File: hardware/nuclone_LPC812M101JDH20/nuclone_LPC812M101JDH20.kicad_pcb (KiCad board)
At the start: 2 copper layers, 48.3 x 48.3 mm, 35 parts, among them J1 JTAG_2X05, J2 Conn_01x02, J3 nuclone_small_left, J4 nuclone_small_right, U1 MCP1702-MB, U2 LPC812M101JDH20, Y1 12MHz

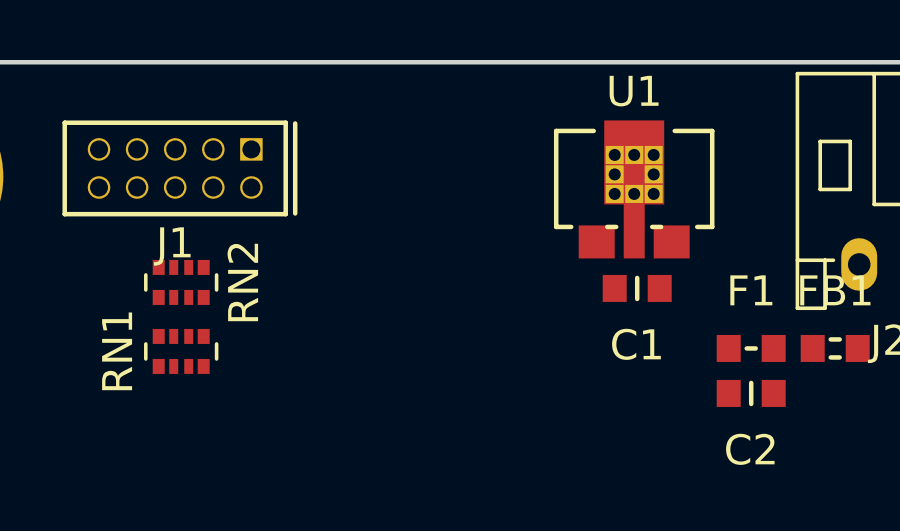
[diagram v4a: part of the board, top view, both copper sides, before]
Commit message: added switch footprints, added reset button
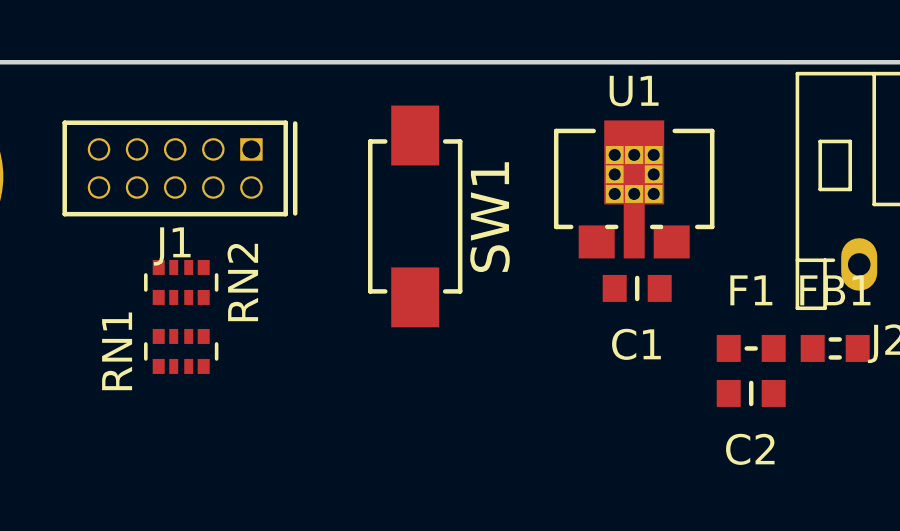
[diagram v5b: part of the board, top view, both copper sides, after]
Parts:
- added SW1: SW_Push, SquantorSwitches:DTSM3, F.Cu at (81.7, 66.1)
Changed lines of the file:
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@@
     (tracks 5)
     (zones 0)
-    (modules 35)
+    (modules 36)
     (nets 57)
   )
@@
     (add_net VSS)
   )
+  (module SquantorSwitches:DTSM3 (layer F.Cu)
+    (at 81.7 66.1 270)
+    (attr smd)
+    (fp_text reference SW1 (at 0 -2.54 90) (layer F.SilkS)
+      (effects (font (size 1.27 1.27) (thickness 0.15)))
+    )
+    (fp_text value SW_Push (at 0 2.54 90) (layer F.Fab)
+      (effects (font (size 1.27 1.27) (thickness 0.15)))
+    )
+    (fp_line (start 2.49936 -1.4986) (end -2.49936 -1.4986) (layer F.SilkS) (width 0.15))
+    (fp_line (start 2.49936 -0.99822) (end 2.49936 -1.4986) (layer F.SilkS) (width 0.15))
+    (fp_line (start 2.49936 1.4986) (end 2.49936 0.99822) (layer F.SilkS) (width 0.15))
+    (fp_line (start -2.49936 1.4986) (end 2.49936 1.4986) (layer F.SilkS) (width 0.15))
+    (fp_line (start -2.49936 0.99822) (end -2.49936 1.4986) (layer F.SilkS) (width 0.15))
+    (fp_line (start -2.49936 -1.4986) (end -2.49936 -0.99822) (layer F.SilkS) (width 0.15))
+    (pad 2 smd rect (at 2.69748 0 270) (size 1.99898 1.59766) (layers F.Cu F.Paste F.Mask)
+      (net 25 /PIO0_5_MCU))
+    (pad 1 smd rect (at -2.69748 0 270) (size 1.99898 1.59766) (layers F.Cu F.Paste F.Mask)
+      (net 5 VSS))
+  )
   (module Resistor_SMD:R_Array_Convex_4x0402 (layer F.Cu)

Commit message: initial routing
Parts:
- moved RN1 0.70 mm to (73.9, 71.3)
- moved C1 0.22 mm to (89.0, 68.7)
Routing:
- net /VBUS: track 0.00 -> 34.5 mm, vias 0 -> 1
- net /VDD: track 0.00 -> 33.1 mm
- net /PIO0_5_MCU: track 0.00 -> 15.2 mm, vias 0 -> 3
- net /PIO0_10_MCU: track 0.00 -> 14.4 mm
- net /PIO0_16_MCU: track 0.00 -> 14.3 mm
- net /PIO0_12_MCU: track 0.00 -> 13.5 mm
- net /PIO0_13_MCU: track 0.00 -> 13.4 mm
- net /PIO0_4_MCU: track 0.00 -> 13.4 mm
- net /PIO0_17_MCU: track 0.00 -> 13.3 mm
- net /PIO0_11_MCU: track 0.00 -> 13.2 mm
- net /PIO0_3: track 0.00 -> 10.5 mm, vias 0 -> 1
- net /PIO0_5: track 0.00 -> 10.5 mm, vias 0 -> 1
- net /PIO0_2: track 0.00 -> 10.2 mm, vias 0 -> 1
- net VSS: track 0.00 -> 9.42 mm, vias 0 -> 4
- net /PIO0_17_OUT: track 0.00 -> 6.44 mm
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- added copper zone on B.Cu, net /VBUS
- added copper zone on F.Cu, net /VBUS

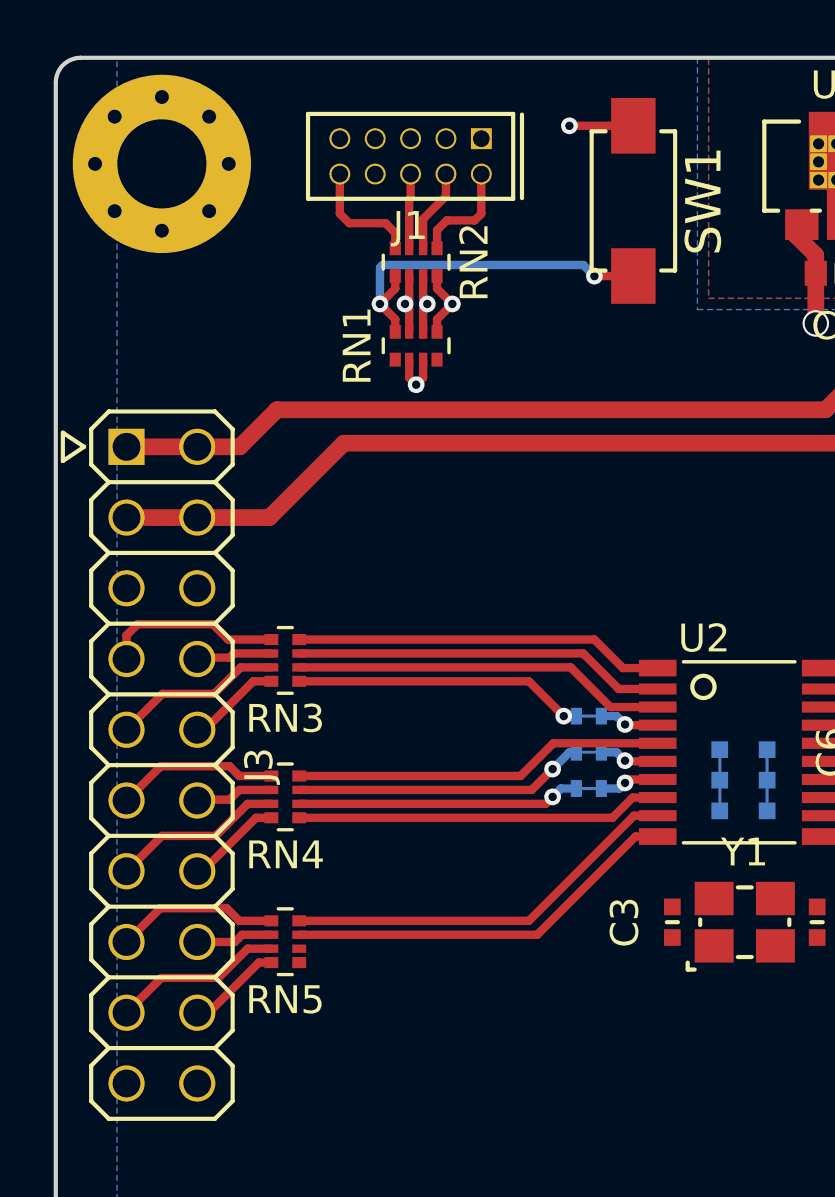
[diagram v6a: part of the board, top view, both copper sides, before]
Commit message: renamed reset button, some silk placement
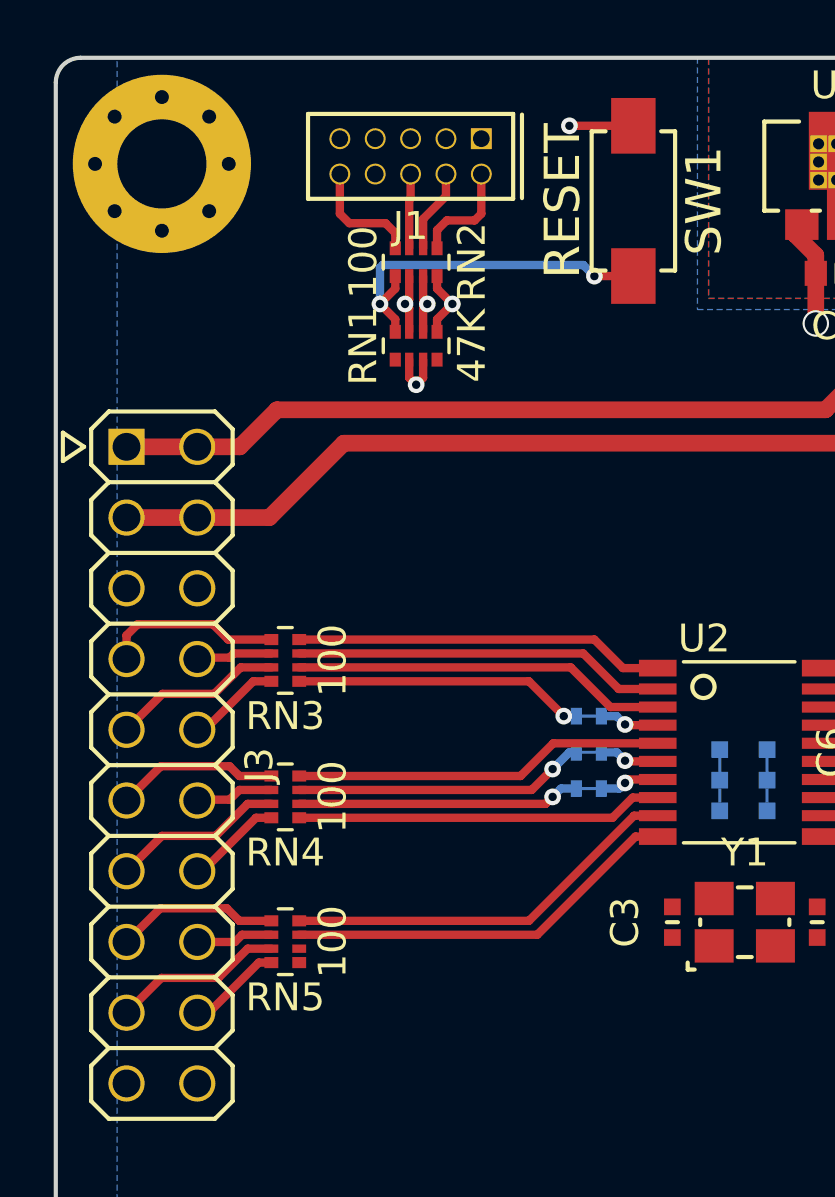
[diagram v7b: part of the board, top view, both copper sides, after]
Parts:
- SW1: value SW_Push -> RESET
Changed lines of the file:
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@@
       (effects (font (size 1.27 1.27) (thickness 0.15)))
     )
-    (fp_text value SW_Push (at 0 2.54 90) (layer F.Fab)
+    (fp_text value RESET (at 0 2.54 90) (layer F.SilkS)
       (effects (font (size 1.27 1.27) (thickness 0.15)))
     )
@@
     (tags "resistor array")
     (attr smd)
-    (fp_text reference RN5 (at 0 -2.1) (layer F.SilkS)
-      (effects (font (size 1 1) (thickness 0.15)))
-    )
-    (fp_text value 100 (at 0 2.1) (layer F.Fab)
+    (fp_text reference RN5 (at 0 -2) (layer F.SilkS)
+      (effects (font (size 1 1) (thickness 0.15)))
+    )
+    (fp_text value 100 (at -1.7 0 90) (layer F.SilkS)
       (effects (font (size 1 1) (thickness 0.15)))
     )
@@
     (tags "resistor array")
     (attr smd)
-    (fp_text reference RN4 (at 0 -2.1) (layer F.SilkS)
-      (effects (font (size 1 1) (thickness 0.15)))
-    )
-    (fp_text value 100 (at 0 2.1) (layer F.Fab)
+    (fp_text reference RN4 (at 0 -2) (layer F.SilkS)
+      (effects (font (size 1 1) (thickness 0.15)))
+    )
+    (fp_text value 100 (at -1.7 0 90) (layer F.SilkS)
       (effects (font (size 1 1) (thickness 0.15)))
     )
@@
     (tags "resistor array")
     (attr smd)
-    (fp_text reference RN3 (at 0 -2.1) (layer F.SilkS)
-      (effects (font (size 1 1) (thickness 0.15)))
-    )
-    (fp_text value 100 (at 0 2.1) (layer F.Fab)
+    (fp_text reference RN3 (at 0 -2) (layer F.SilkS)
+      (effects (font (size 1 1) (thickness 0.15)))
+    )
+    (fp_text value 100 (at -1.7 0 90) (layer F.SilkS)
       (effects (font (size 1 1) (thickness 0.15)))
     )
@@
     (tags "resistor array")
     (attr smd)
-    (fp_text reference RN2 (at 0 -2.1 90) (layer F.SilkS)
-      (effects (font (size 1 1) (thickness 0.15)))
-    )
-    (fp_text value 100 (at 0 2.1 90) (layer F.Fab)
+    (fp_text reference RN2 (at 0 -2 90) (layer F.SilkS)
+      (effects (font (size 1 1) (thickness 0.15)))
+    )
+    (fp_text value 100 (at 0 1.9 90) (layer F.SilkS)
       (effects (font (size 1 1) (thickness 0.15)))
     )
@@
     (tags "resistor array")
     (attr smd)
-    (fp_text reference RN1 (at 0 -2.1 90) (layer F.SilkS)
-      (effects (font (size 1 1) (thickness 0.15)))
-    )
-    (fp_text value 47K (at 0 2.1 90) (layer F.Fab)
-      (effects (font (size 1 1) (thickness 0.15)))
-    )
+    (fp_text reference RN1 (at 0 -1.9 90) (layer F.SilkS)
+      (effects (font (size 1 1) (thickness 0.15)))
+    )
+    (fp_text value 47K (at 0 2 90) (layer F.SilkS)
+      (effects (font (size 1 1) (thickness 0.15)))
+    )

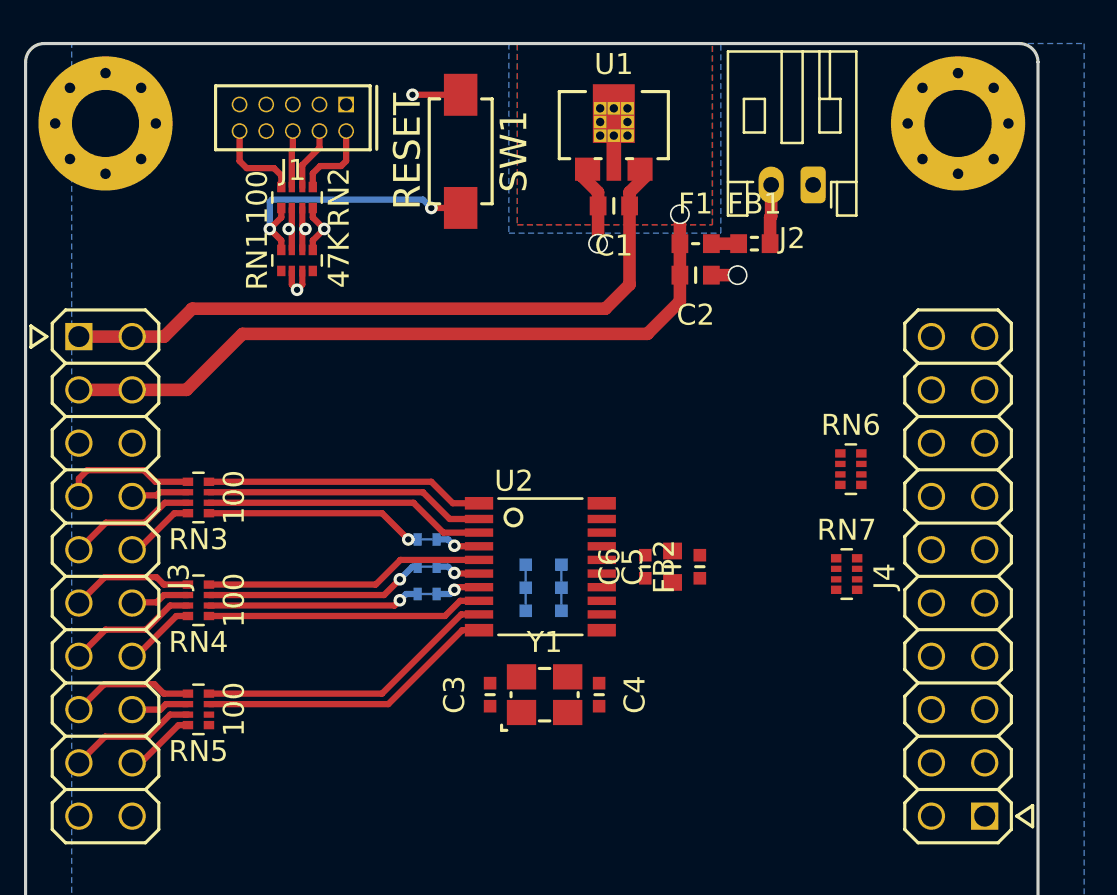
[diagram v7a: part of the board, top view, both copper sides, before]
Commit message: routing futher completed, added net classes
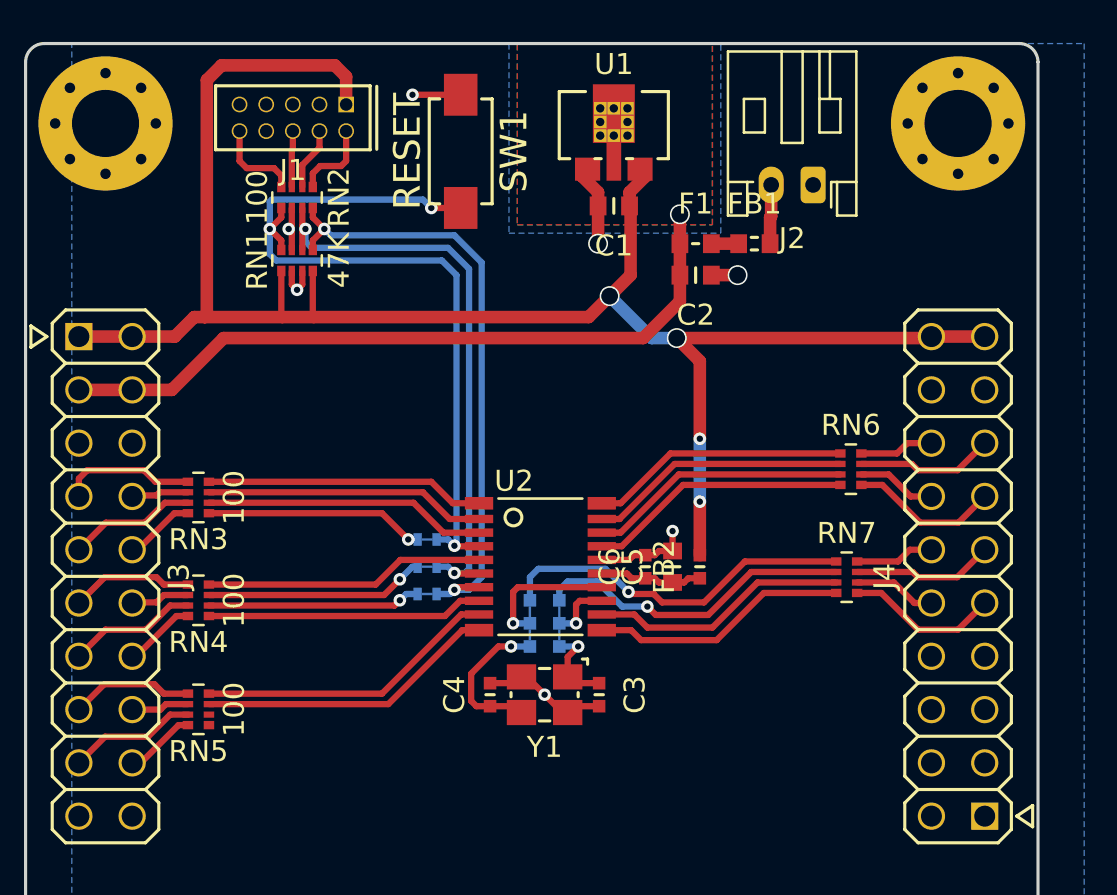
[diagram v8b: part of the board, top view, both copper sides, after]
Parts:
- moved C3 5.20 mm to (88.3, 92.0), turned to 270 degrees
- moved C4 5.20 mm to (83.1, 92.0), turned to 90 degrees
- moved JP5 2.33 mm to (86.4, 88.6)
- moved JP4 2.27 mm to (85.0, 88.6)
- moved RN7 0.15 mm to (100.1, 86.4)
- turned Y1 to 180 degrees
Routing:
- net /VDD: track 33.1 -> 86.7 mm, vias 0 -> 4
- net /PIO0_2_MCU: track 4.62 -> 29.3 mm
- net /PIO0_3_MCU: track 4.28 -> 28.3 mm
- net /PIO0_5_MCU: track 15.2 -> 38.7 mm
- net /PIO0_8: track 0.00 -> 17.3 mm, vias 0 -> 1
- net /PIO0_9: track 0.00 -> 15.4 mm, vias 0 -> 1
- net /PIO0_7_MCU: track 0.00 -> 12.6 mm
- net /PIO0_6_MCU: track 0.00 -> 12.5 mm
- net /PIO0_0_MCU: track 0.00 -> 12.5 mm
- net /PIO0_14_MCU: track 0.00 -> 12.4 mm
- net /PIO0_1_MCU: track 0.00 -> 12.3 mm
- net /PIO0_15_MCU: track 0.00 -> 12.3 mm
- net VSS: track 9.42 -> 20.1 mm, vias 4 -> 6
- net /PIO0_15_OUT: track 0.00 -> 7.33 mm
- net /XTAL_OUT: track 0.00 -> 7.27 mm, vias 0 -> 1
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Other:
- net class Power added: clearance 0.127, trace_width 0.6, via_dia 1.1, via_drill 0.8
- net class Signal added: clearance 0.127, trace_width 0.3, via_dia 0.6, via_drill 0.3
